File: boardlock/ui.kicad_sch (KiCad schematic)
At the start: 3 parts, among them J1 USB_C_Receptacle_USB2.0

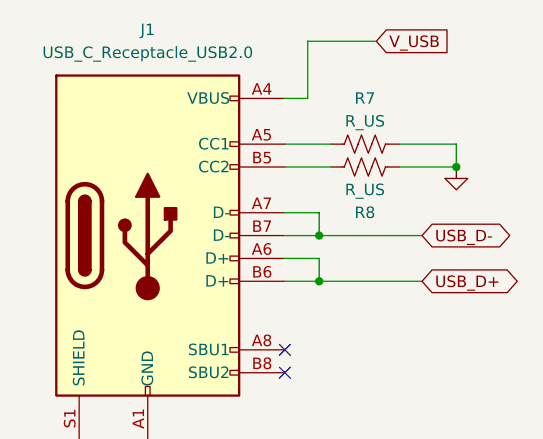
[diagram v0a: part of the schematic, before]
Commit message: added buck boost topology
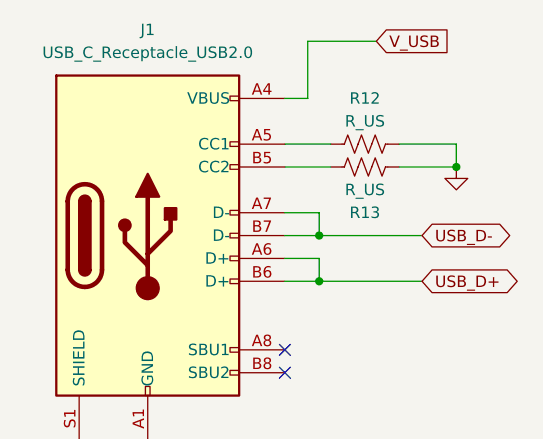
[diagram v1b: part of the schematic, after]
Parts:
- renumbered R7 to R12, R8 to R13
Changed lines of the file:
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@@
   (symbol (lib_id "power:GND") (at 40.64 78.74 0) (unit 1)
     (in_bom yes) (on_board yes) (dnp no) (fields_autoplaced)
-    (property "Reference" "#PWR09" (at 40.64 85.09 0)
+    (property "Reference" "#PWR028" (at 40.64 85.09 0)
       (effects (font (size 1.27 1.27)) hide)
     )
@@
       (project "boardlock"
         (path "/e1fc29ce-837e-4062-84d8-c7e423f9eab9/c1e95beb-a482-4f8e-b13b-3641abb17f9b"
-          (reference "#PWR09") (unit 1)
+          (reference "#PWR028") (unit 1)
         )
       )
@@
   (symbol (lib_id "Device:R_US") (at 72.39 45.72 270) (unit 1)
     (in_bom yes) (on_board yes) (dnp no)
-    (property "Reference" "R8" (at 72.39 50.8 90)
+    (property "Reference" "R13" (at 72.39 50.8 90)
       (effects (font (size 1.27 1.27)))
     )
@@
       (project "boardlock"
         (path "/e1fc29ce-837e-4062-84d8-c7e423f9eab9/c1e95beb-a482-4f8e-b13b-3641abb17f9b"
-          (reference "R8") (unit 1)
+          (reference "R13") (unit 1)
         )
       )
@@
   (symbol (lib_id "Device:R_US") (at 72.39 43.18 90) (unit 1)
     (in_bom yes) (on_board yes) (dnp no)
-    (property "Reference" "R7" (at 72.39 38.1 90)
+    (property "Reference" "R12" (at 72.39 38.1 90)
       (effects (font (size 1.27 1.27)))
     )
@@
       (project "boardlock"
         (path "/e1fc29ce-837e-4062-84d8-c7e423f9eab9/c1e95beb-a482-4f8e-b13b-3641abb17f9b"
-          (reference "R7") (unit 1)
+          (reference "R12") (unit 1)
         )
       )
@@
   (symbol (lib_id "power:GND") (at 82.55 45.72 0) (unit 1)
     (in_bom yes) (on_board yes) (dnp no)
-    (property "Reference" "#PWR022" (at 82.55 52.07 0)
+    (property "Reference" "#PWR029" (at 82.55 52.07 0)
       (effects (font (size 1.27 1.27)) hide)
     )
@@
       (project "boardlock"
         (path "/e1fc29ce-837e-4062-84d8-c7e423f9eab9/c1e95beb-a482-4f8e-b13b-3641abb17f9b"
-          (reference "#PWR022") (unit 1)
+          (reference "#PWR029") (unit 1)
         )
       )

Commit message: More zecong edits
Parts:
- J?: renamed from J1; footprint (none) -> Connector_USB:USB_C_Receptacle_JAE_DX07S016JA1R1500; MFN Part # (none) -> DX07S016JA1R1500
- R12, R13: value R_US -> 5.1k
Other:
- company: (none) -> Schetmatic
- title: (none) -> BoardLock Schematic
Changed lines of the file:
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@@
 (kicad_sch (version 20230121) (generator eeschema)
   (paper "A4")
+  (title_block
+    (title "BoardLock Schematic")
+    (rev "Rev1")
+    (company "Schetmatic")
+  )
   (junction (at 40.64 77.47) (diameter 0) (color 0 0 0 0)
   )
@@
       (effects (font (size 1.27 1.27)))
     )
-    (property "Value" "R_US" (at 72.39 48.26 90)
+    (property "Value" "5.1k" (at 72.39 48.26 90)
       (effects (font (size 1.27 1.27)))
     )
@@
       (effects (font (size 1.27 1.27)))
     )
-    (property "Value" "R_US" (at 72.39 40.64 90)
+    (property "Value" "5.1k" (at 72.39 40.64 90)
       (effects (font (size 1.27 1.27)))
     )
@@
   )
   (symbol (lib_id "Connector:USB_C_Receptacle_USB2.0") (at 48.26 53.34 0) (unit 1)
-    (in_bom yes) (on_board yes) (dnp no) (fields_autoplaced)
-    (property "Reference" "J1" (at 48.26 30.48 0)
-      (effects (font (size 1.27 1.27)))
-    )
-    (property "Value" "USB_C_Receptacle_USB2.0" (at 48.26 33.02 0)
-      (effects (font (size 1.27 1.27)))
-    )
-    (property "Footprint" "" (at 52.07 53.34 0)
-      (effects (font (size 1.27 1.27)) hide)
-    )
-    (property "Datasheet" "https://www.usb.org/sites/default/files/documents/usb_type-c.zip" (at 52.07 53.34 0)
-      (effects (font (size 1.27 1.27)) hide)
+    (in_bom yes) (on_board yes) (dnp no)
+    (property "Reference" "J?" (at 48.26 27.94 0)
+      (effects (font (size 1.27 1.27)))
+    )
+    (property "Value" "USB_C_Receptacle_USB2.0" (at 48.26 30.48 0)
+      (effects (font (size 1.27 1.27)))
+    )
+    (property "Footprint" "Connector_USB:USB_C_Receptacle_JAE_DX07S016JA1R1500" (at 52.07 53.34 0)
+      (effects (font (size 1.27 1.27)) hide)
+    )
+    (property "Datasheet" "https://www.digikey.com/en/products/detail/jae-electronics/dx07s016ja1r1500/11585731" (at 52.07 53.34 0)
+      (effects (font (size 1.27 1.27)) hide)
+    )
+    (property "MFN Part #" "DX07S016JA1R1500" (at 48.26 33.02 0)
+      (effects (font (size 1.27 1.27)))
     )
     (pin "A1")
@@
       (project "boardlock"
         (path "/e1fc29ce-837e-4062-84d8-c7e423f9eab9/c1e95beb-a482-4f8e-b13b-3641abb17f9b"
-          (reference "J1") (unit 1)
-        )
-      )
+          (reference "J?") (unit 1)
+        )
+      )

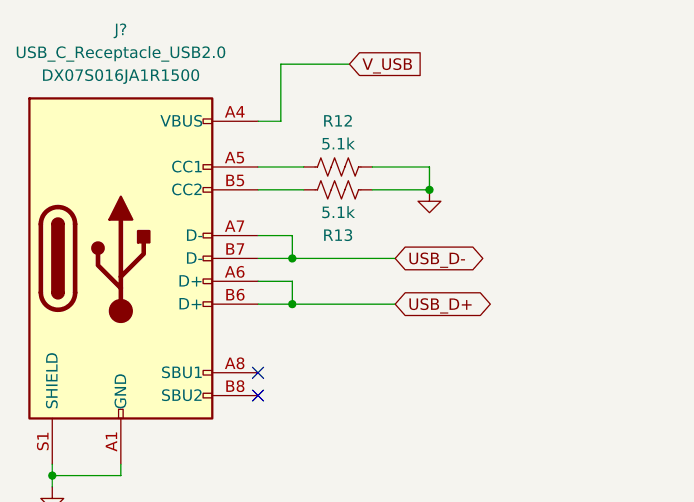
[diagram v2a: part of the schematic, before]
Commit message: Added 1 USB protection diode
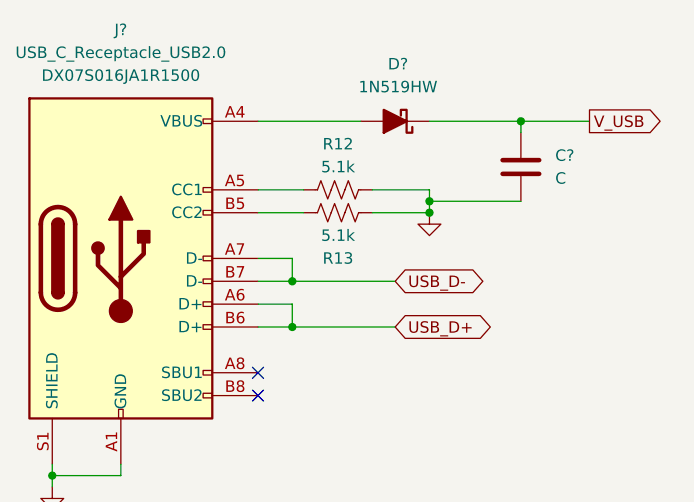
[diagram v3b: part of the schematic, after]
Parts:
- added C?: C, symbol Device:C
- added D?: 1N519HW, Diode_SMD:D_SOD-123, symbol Device:D_Schottky_Filled
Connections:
- net GND: now also C?.2
- net V_USB: now also C?.1, D?.1 (K); no longer J?.A4 (VBUS), J?.A9 (VBUS), J?.B4 (VBUS), J?.B9 (VBUS)
- new net: D?.2 (A), J?.A4 (VBUS), J?.A9 (VBUS), J?.B4 (VBUS), J?.B9 (VBUS)
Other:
- moved on the sheet: R12, R13

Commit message: more Zecong edits
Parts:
- removed C?: C, symbol Device:C
- added C?: 10uF, symbol Device:C
- added U?: TPD2E2U06, Package_TO_SOT_SMD:SOT-543, symbol Power_Protection:TPD2E2U06
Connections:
- net GND: now also C?.2, U?.4
- net USB_D+: now also U?.3
- net USB_D-: now also U?.5
- net V_USB: now also D?.2 (A), J?.A4 (VBUS), J?.A9 (VBUS), J?.B4 (VBUS), J?.B9 (VBUS); no longer D?.1 (K)
- new net VBUS: C?.1, D?.1 (K)
- no-connect marks 2 -> 4
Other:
- note added: "TVS Diodes for ESP Protection"
- note added: "USB-C Connector in USB 2.0 Mode"
- moved on the sheet: D?, J?, R12, R13

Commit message: buttons and stuff
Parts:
- added C23, C24: 0.1uF, symbol Device:C_Small
- added D2: CLVBA-FKA-CC1F1L1BB7R3R3D, symbol Device:LED_RABG
- added R18: 175, symbol Device:R_Small_US
- added R19, R20: 40, symbol Device:R_Small_US
- added R21, R22: 10k, symbol Device:R_Small_US
- added R22 (x2): 1k, symbol Device:R_Small_US
- added SW1 (x3), SW2: SW_Push, symbol Switch:SW_Push
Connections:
- net GND: now also C23.2, C24.2, SW1.1, SW2.1
- new net: D2.1 (RK), R18.1
- new net: D2.3 (BK), R20.1
- new net: D2.4 (GK), R19.1
- new net: R22.1, SW1.2 (x2)
- new net +3V3: D2.2 (A), R21.1, R22.1, SW1.1, SW1.1
- new net M_BOOT: C24.1, R22.2, SW2.2
- new net M_BUTTON_EXT: R22.2
- new net M_BUTTON_INT: R22.2
- new net M_RGB_B: R20.2
- new net M_RGB_G: R19.2
- new net M_RGB_R: R18.2
- new net M_RST_N: C23.1, R21.2, SW1.2
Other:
- note added: "assuming using big LED, change pin order if not"
- note added: "check other circuitry in dev kit schematic to see if it's needed for RST and BOOT"
- note added: "may need to enable pull-downs in code based on this configuration"
- note added: "maybe 100k"
- note added: "uC dev kit has 2 caps"

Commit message: lab updates
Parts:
- removed R18: 175, symbol Device:R_Small_US
- removed R19, R20: 40, symbol Device:R_Small_US
- removed R21, R22: 10k, symbol Device:R_Small_US
- removed R22 (x2): 1k, symbol Device:R_Small_US
- removed SW1: SW_Push, symbol Switch:SW_Push
- added C23 (x3): 0.1uF, symbol Device:C_Small
- added Q5, Q6, Q7: MMBT4401, symbol Simulation_SPICE:NPN
- added R18, R23: 10k, symbol Device:R_US
- added R20, R21, R22: 1k, symbol Device:R_US
- added R30, R31, R32, R33, R34, R35, R36, R37, R39: R_US, symbol Device:R_US
- added SW1 (x2): SW_Push, symbol Switch:SW_Push
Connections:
- net +3V3: now also R18.1, R23.1, SW1.1, SW1.1
- net GND: now also C23.2, C23.2, C23.2, Q5.3 (E), Q6.3 (E), Q7.3 (E), R30.2, R35.2, R39.2
- net M_BOOT: now also R18.2
- net M_BUTTON_INT: now also C23.1, R22.2
- net M_RGB_B: now also R36.1
- net M_RGB_G: now also R33.1
- net M_RGB_R: now also R32.1
- net M_RST_N: now also R23.2
- net at D2.1 (RK): now also R31.1
- net at D2.3 (BK): now also R37.1
- net at D2.4 (GK): now also R34.1
- net at SW1.2: now also R20.1
- new net: Q6.1 (C), R34.2
- new net: Q6.2 (B), R30.1, R33.2
- new net: R21.1, SW1.2
- new net: Q5.1 (C), R31.2
- new net: Q5.2 (B), R32.2, R39.1
- new net: R22.1, SW1.2
- new net: Q7.1 (C), R37.2
- new net: Q7.2 (B), R35.1, R36.2
- new net M_BUTTON_EXT1: C23.1, R20.2
- new net M_BUTTON_EXT2: C23.1, R21.2
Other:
- note added: "- check resistors that are in lab - figure out values needed"
- note added: "is boot typically high"
- note removed: "may need to enable pull-downs in code based on this configuration"
- moved on the sheet: SW1

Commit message: not sure what I changed
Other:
- moved on the sheet: C23, C24, D2, Q5, Q6, Q7, R18, R20, R21, R22, R23, R30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

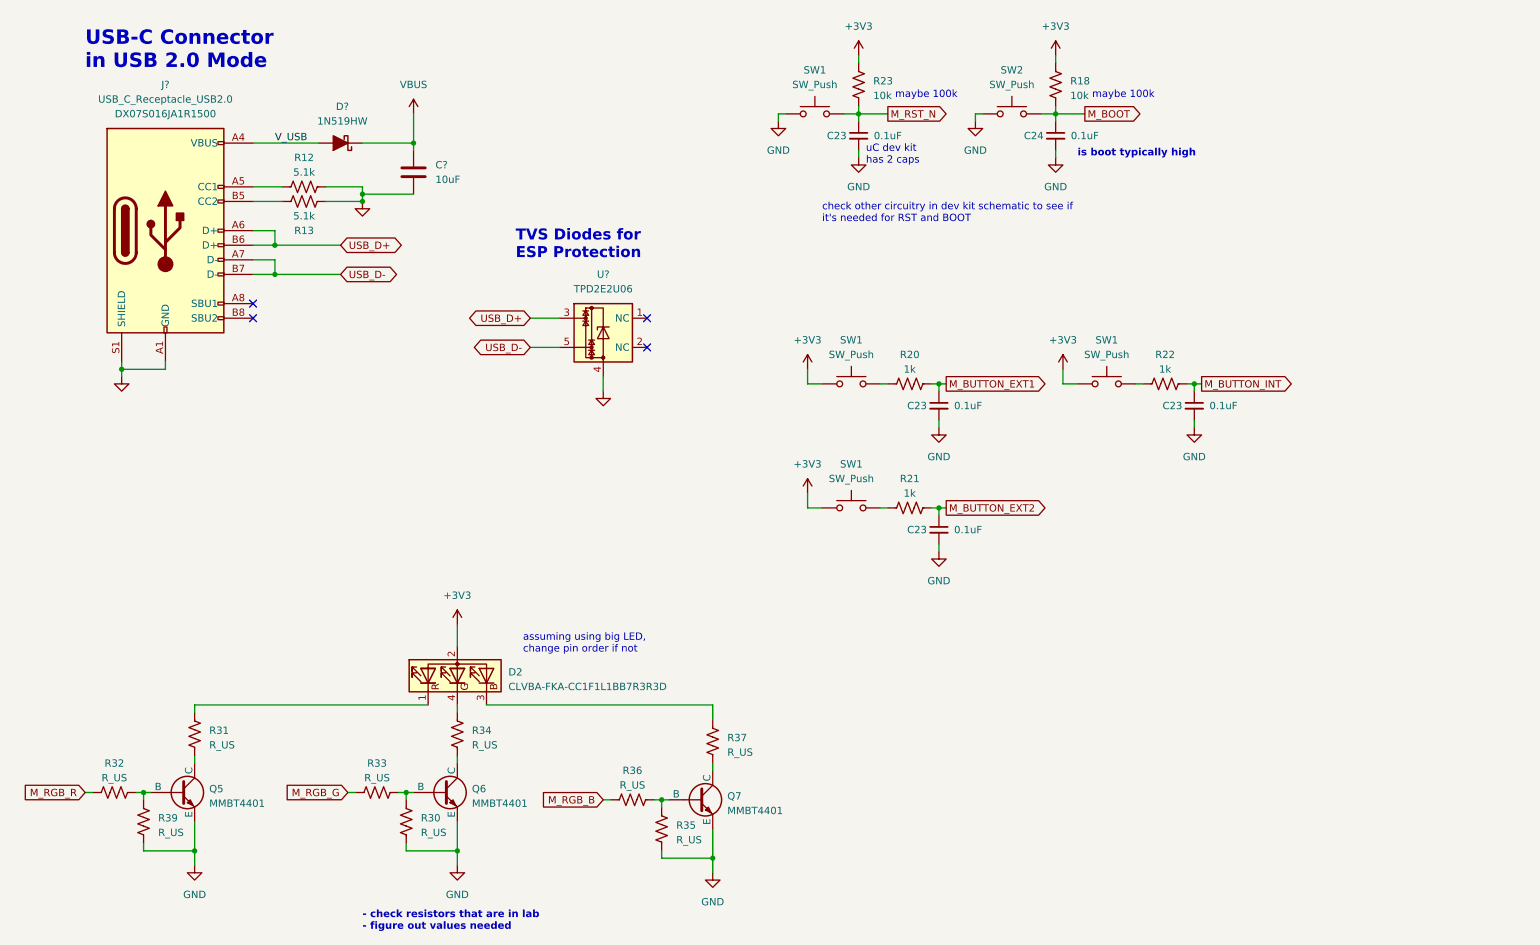
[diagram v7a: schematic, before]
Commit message: added footprints and an LPF to audio
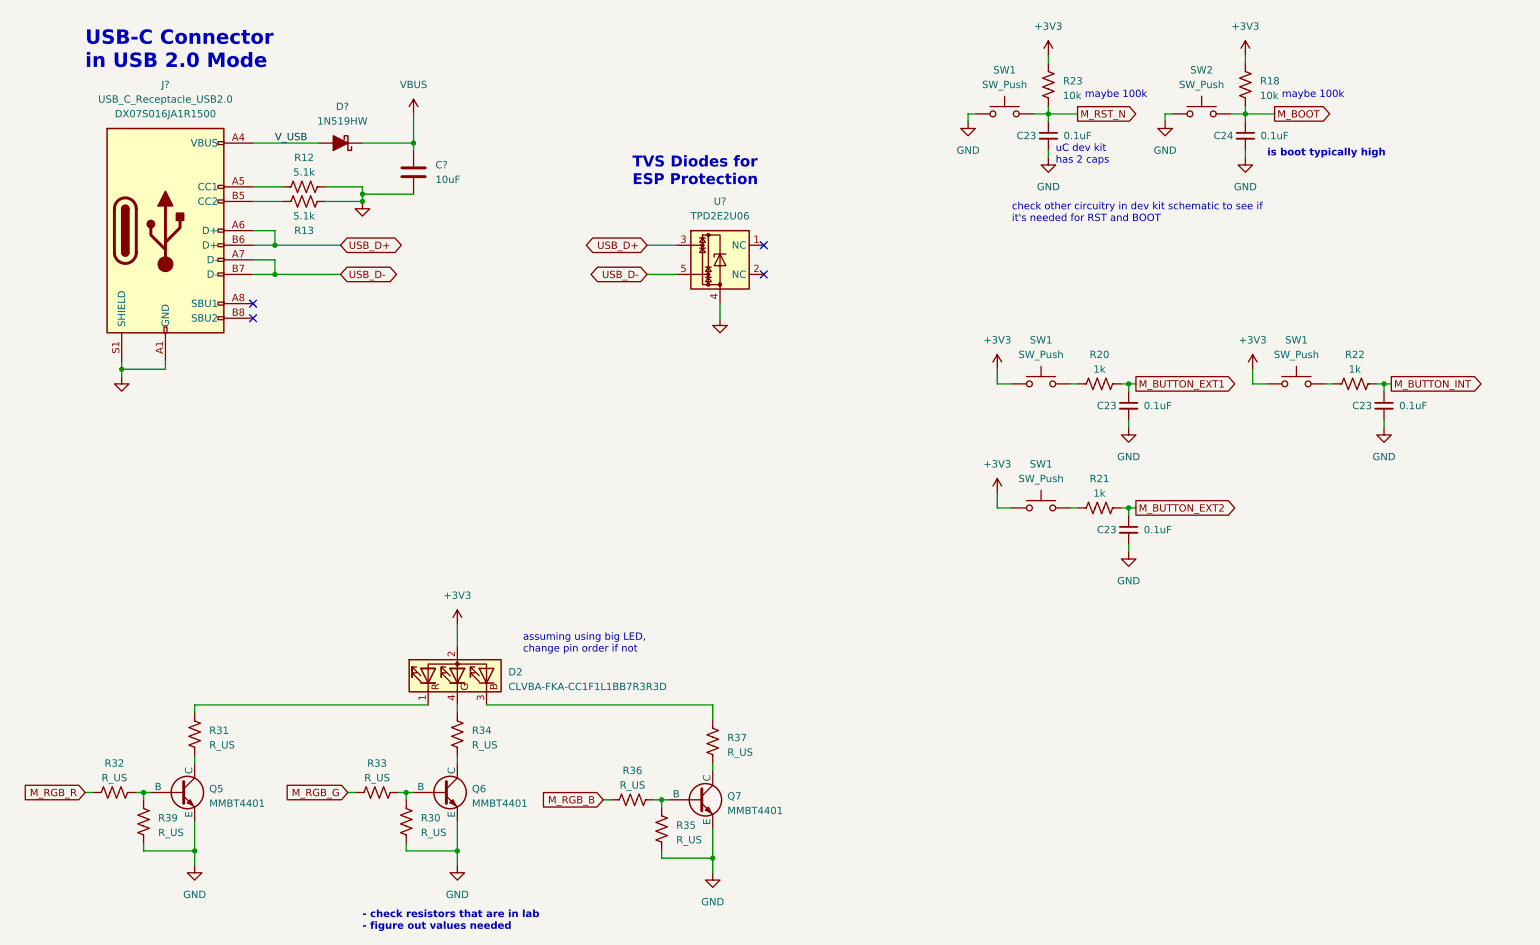
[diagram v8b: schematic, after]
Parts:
- R12, R13, R18, R20, R21, R22, R23, R30, R31, R32, R33, R34, R35, R36, R37: footprint (none) -> Resistor_SMD:R_0805_2012Metric_Pad1.20x1.40mm_HandSolder
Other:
- moved on the sheet: C23, C24, R18, R20, R21, R22, R23, SW1, SW2, U?
